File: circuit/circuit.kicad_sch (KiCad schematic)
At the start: 26 parts, among them SW101 Pedal_1, SW102 Pedal_2, SW103 Pedal_3, SW104 Pedal_4, SW105 Pedal_5, SW106 Pedal_6, SW107 Pedal_7, SW108 Pedal_8, SW109 Program, SW110 Preset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

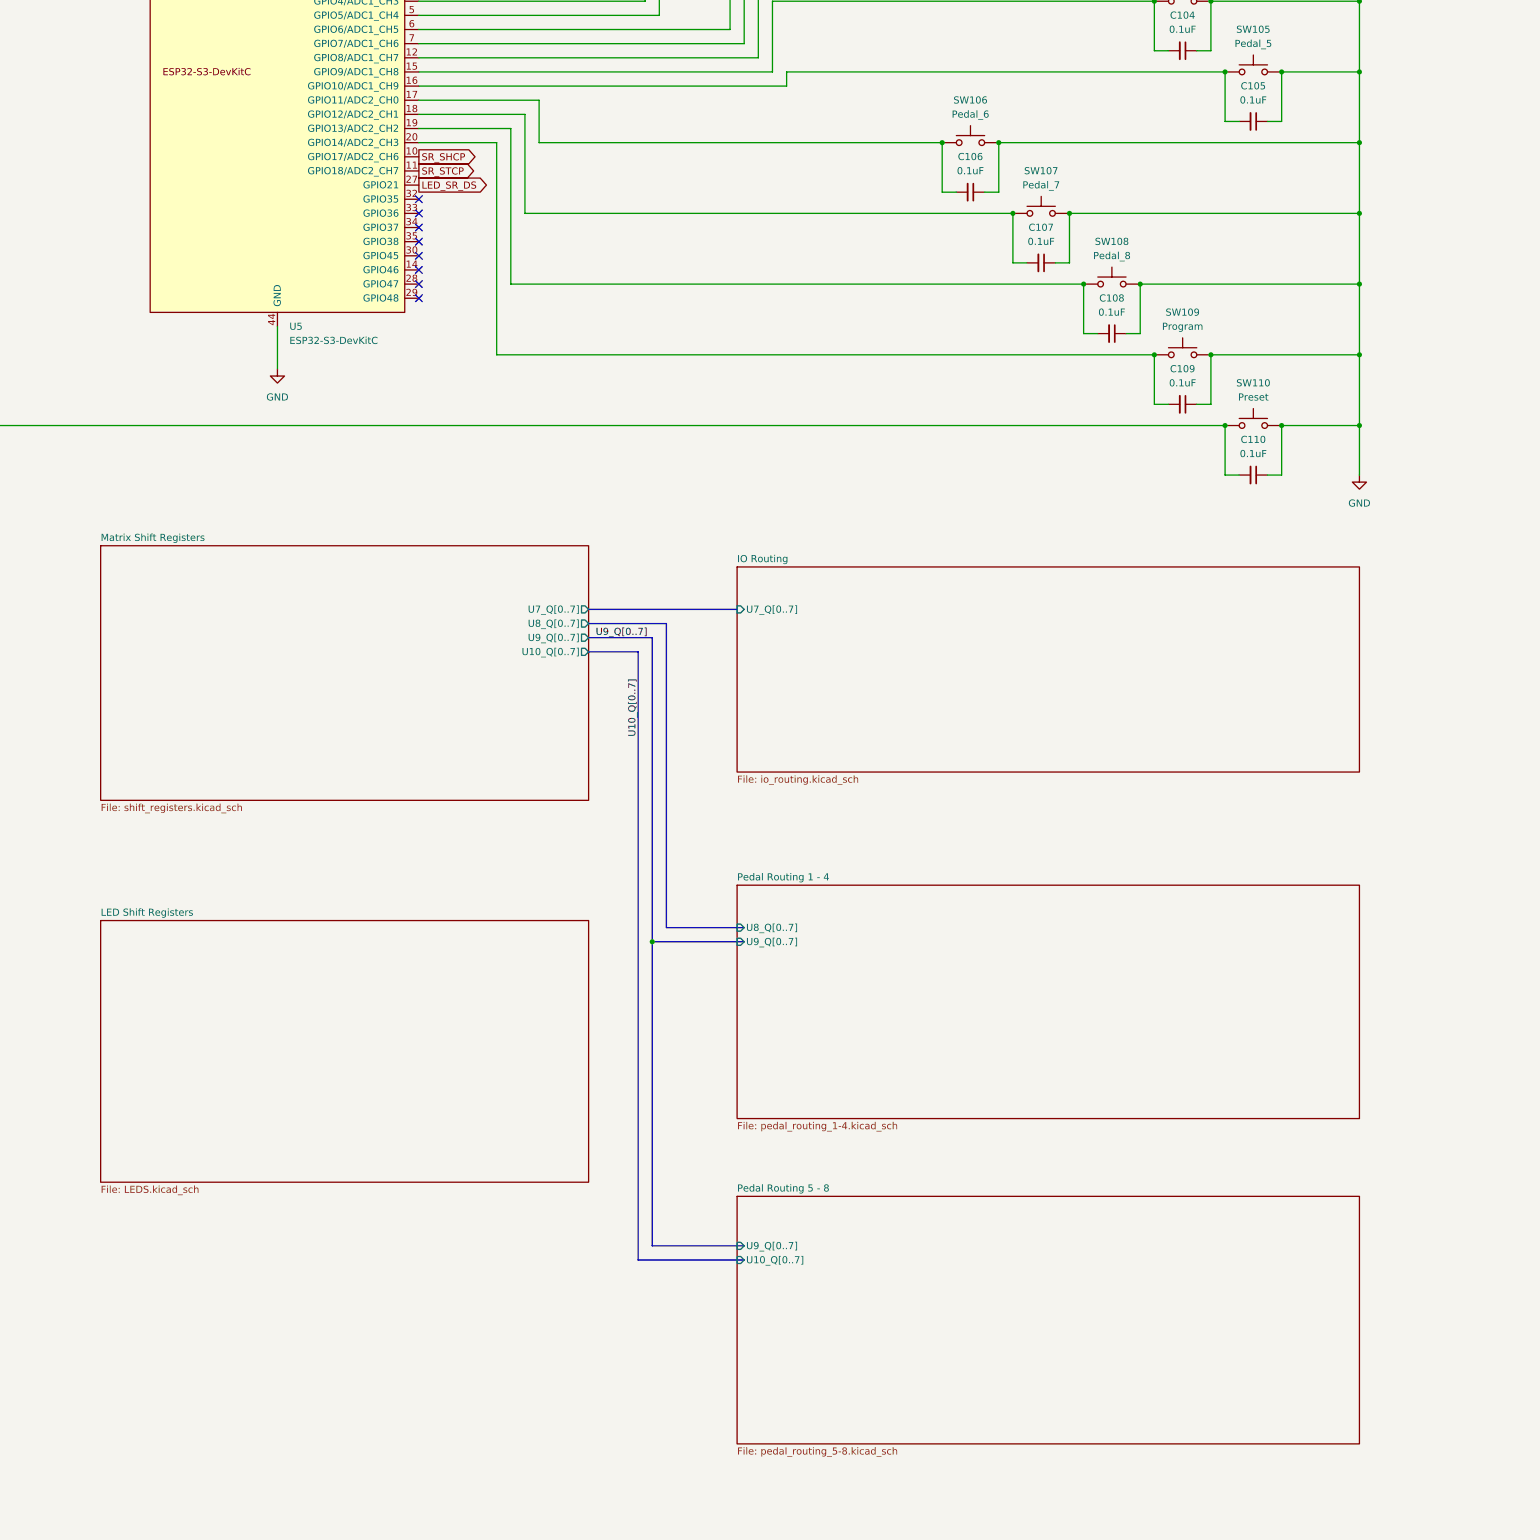
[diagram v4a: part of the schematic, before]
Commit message: Rebuilt Matrix and added inhibit function.
Matrix was flawed, It now supports 8 FX loops (pedals) in any order. Or optionally none at all with a buffered bypass, or anywhere in between. The inhibit function will allow the option to press any loop foot switch an enable or disable it without reprogramming.
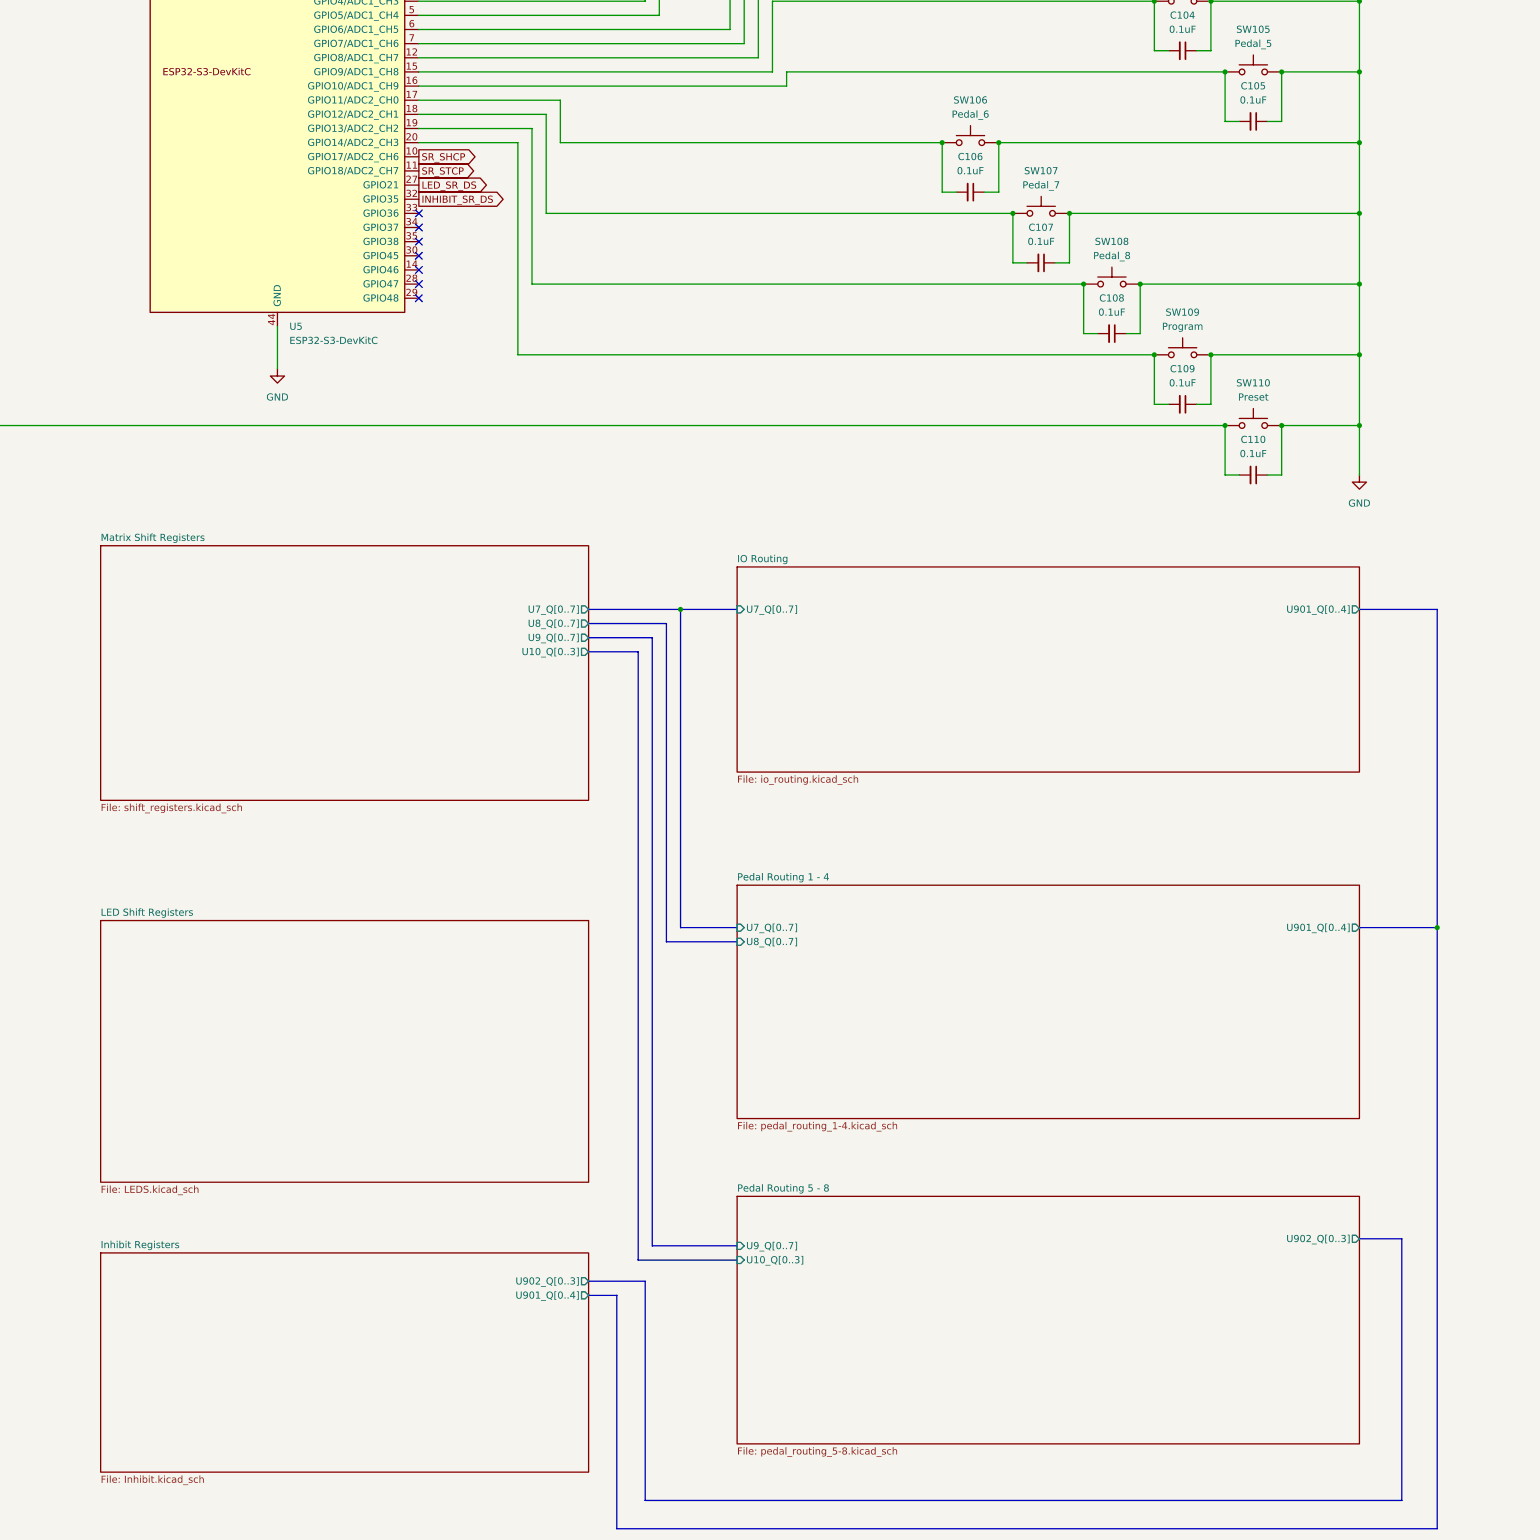
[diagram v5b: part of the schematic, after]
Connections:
- net INHIBIT_SR_DS: now reaches U5.32 (GPIO35)
- no-connect marks 21 -> 20
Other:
- added sheet Inhibit Registers (Inhibit.kicad_sch)
- sheet IO Routing ports: added U901_Q[0..4]; removed none
- sheet Matrix Shift Registers ports: added U10_Q[0..3]; removed U10_Q[0..7]
- sheet Pedal Routing 1 - 4 ports: added U7_Q[0..7], U901_Q[0..4]; removed U9_Q[0..7]
- sheet Pedal Routing 5 - 8 ports: added U10_Q[0..3], U902_Q[0..3]; removed U10_Q[0..7]

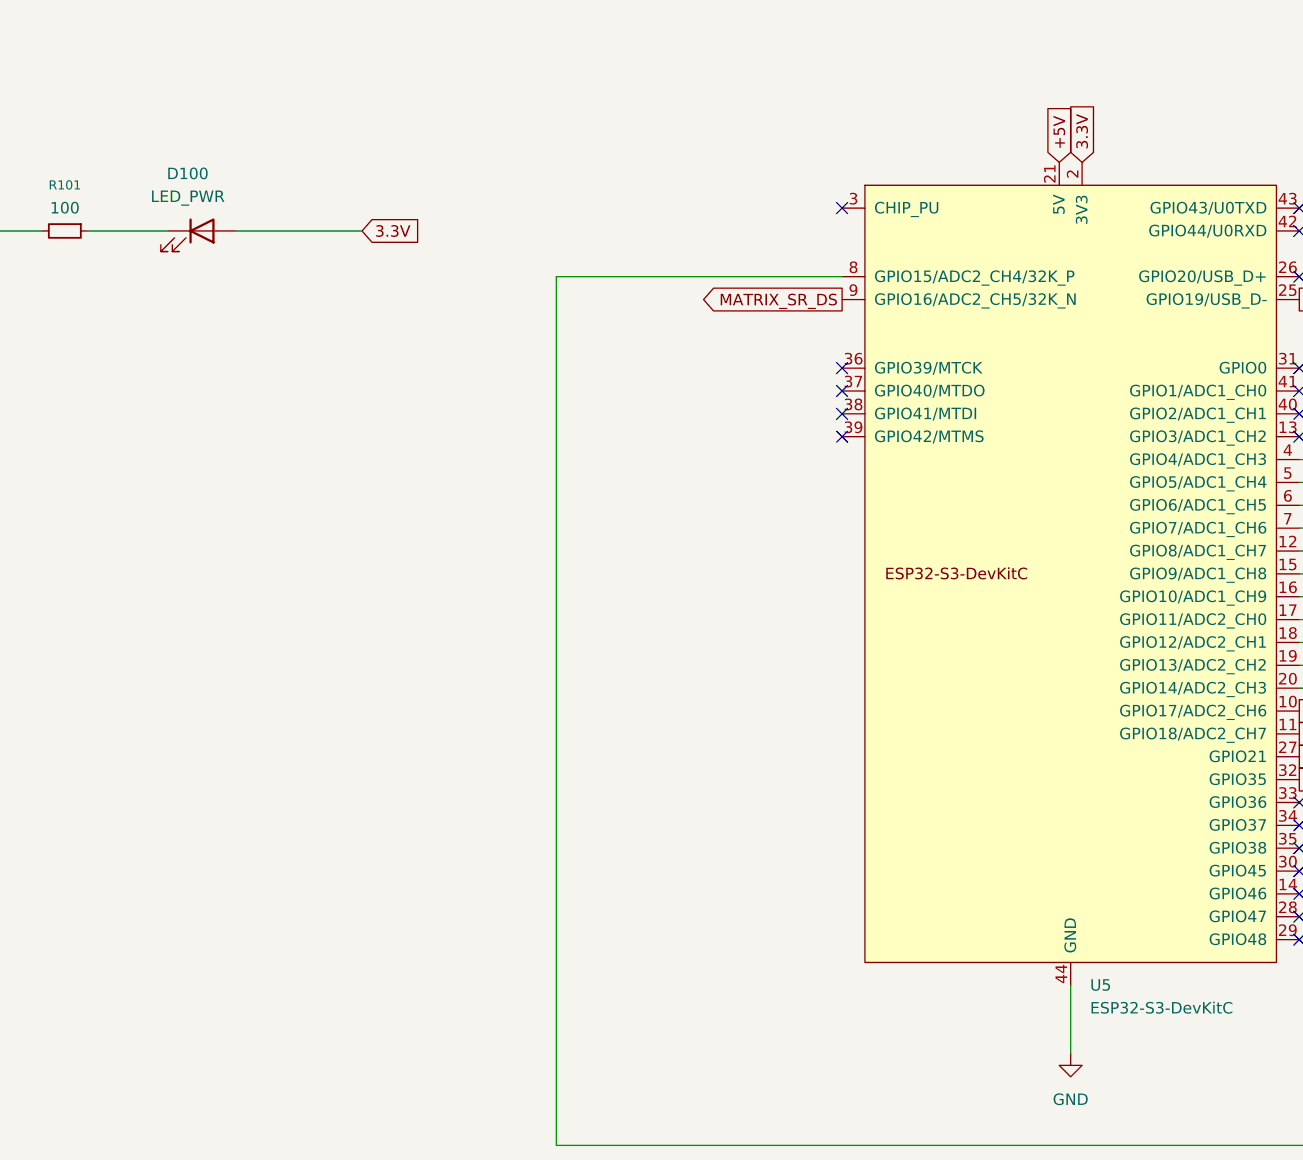
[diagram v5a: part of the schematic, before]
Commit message: Re-annotation of circuit, new PCB routing, updated PDF
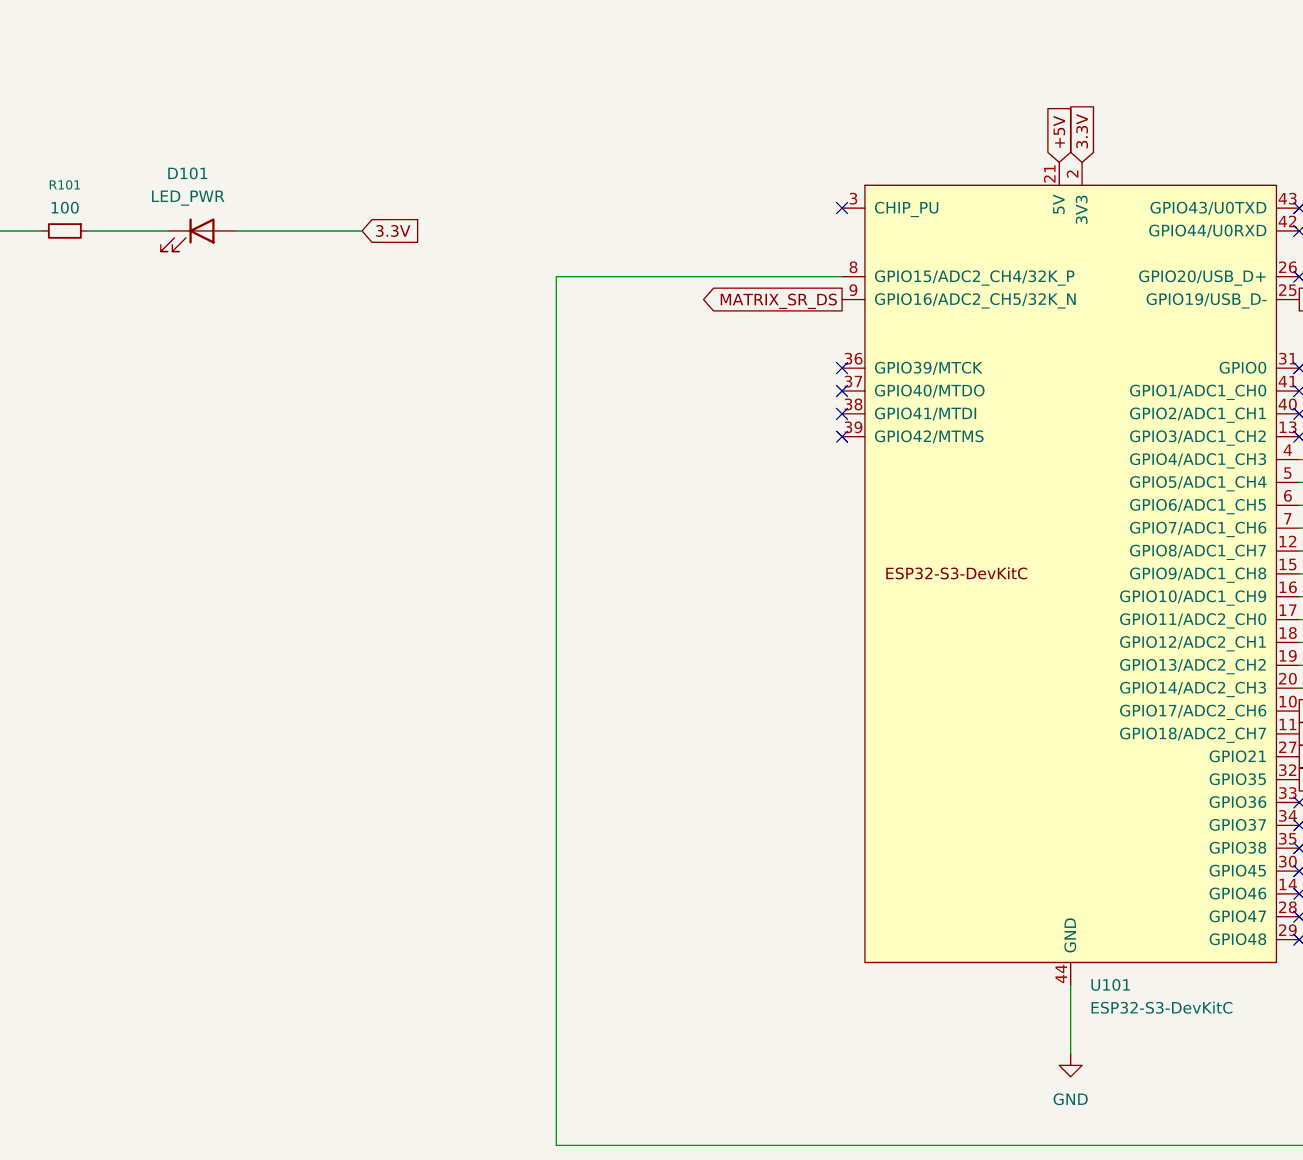
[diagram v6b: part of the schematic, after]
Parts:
- renumbered D100 to D101, U5 to U101
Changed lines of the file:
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@@
 		(dnp no)
 		(fields_autoplaced yes)
-		(property "Reference" "#PWR0105"
+		(property "Reference" "#PWR0110"
 			(at 349.25 180.34 0)
 			(effects
@@
 			(project "circuit"
 				(path "/420e3d7a-6c9a-4806-b4be-05d56aeb21de"
-					(reference "#PWR0105")
+					(reference "#PWR0110")
 					(unit 1)
 				)
@@
 		(dnp no)
 		(fields_autoplaced yes)
-		(property "Reference" "U5"
+		(property "Reference" "U101"
 			(at 157.0833 147.32 0)
 			(effects
@@
 			(project ""
 				(path "/420e3d7a-6c9a-4806-b4be-05d56aeb21de"
-					(reference "U5")
+					(reference "U101")
 					(unit 1)
 				)
@@
 		(dnp no)
 		(fields_autoplaced yes)
-		(property "Reference" "D100"
+		(property "Reference" "D101"
 			(at 56.8325 57.15 0)
 			(effects
@@
 			(project ""
 				(path "/420e3d7a-6c9a-4806-b4be-05d56aeb21de"
-					(reference "D100")
+					(reference "D101")
 					(unit 1)
 				)
@@
 		(dnp no)
 		(fields_autoplaced yes)
-		(property "Reference" "#PWR0110"
+		(property "Reference" "#PWR0104"
 			(at 30.48 77.47 0)
 			(effects
@@
 			(project ""
 				(path "/420e3d7a-6c9a-4806-b4be-05d56aeb21de"
-					(reference "#PWR0110")
+					(reference "#PWR0104")
 					(unit 1)
 				)
@@
 		(dnp no)
 		(fields_autoplaced yes)
-		(property "Reference" "#FLG0102"
+		(property "Reference" "#FLG0101"
 			(at 374.015 38.1 0)
 			(effects
@@
 			(project "circuit"
 				(path "/420e3d7a-6c9a-4806-b4be-05d56aeb21de"
-					(reference "#FLG0102")
+					(reference "#FLG0101")
 					(unit 1)
 				)
@@
 		(dnp no)
 		(fields_autoplaced yes)
-		(property "Reference" "#FLG0101"
+		(property "Reference" "#FLG0102"
 			(at 387.985 38.1 0)
 			(effects
@@
 			(project "circuit"
 				(path "/420e3d7a-6c9a-4806-b4be-05d56aeb21de"
-					(reference "#FLG0101")
+					(reference "#FLG0102")
 					(unit 1)
 				)
@@
 		(dnp no)
 		(fields_autoplaced yes)
-		(property "Reference" "#PWR0104"
+		(property "Reference" "#PWR0105"
 			(at 154.94 161.29 0)
 			(effects
@@
 			(project ""
 				(path "/420e3d7a-6c9a-4806-b4be-05d56aeb21de"
-					(reference "#PWR0104")
-					(unit 1)
-				)
+					(reference "#PWR0105")
+					(unit 1)
+				)
